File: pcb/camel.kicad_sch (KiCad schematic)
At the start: 54 parts, among them J1 Conn_01x04, J2 Conn_01x04, J3 TC2030-NL, J4 USART, J5 Conn_01x04, J6 I2C STEMMA, U1 MCP1700T-3302E/TT, U2 HX712, U3 STM32L010F4P6, U4 HX712

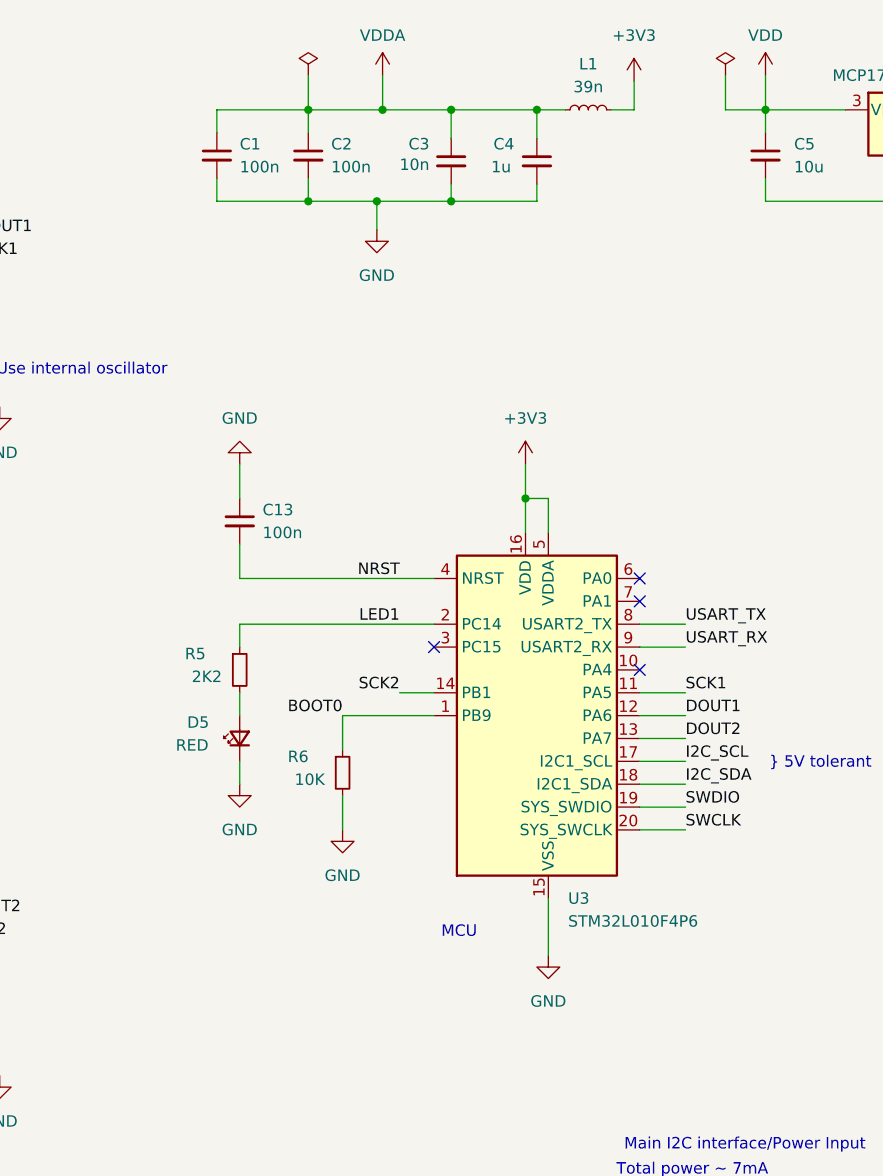
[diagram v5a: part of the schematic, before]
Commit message: updated STM32CubeMX version, updating to STM32L031F6
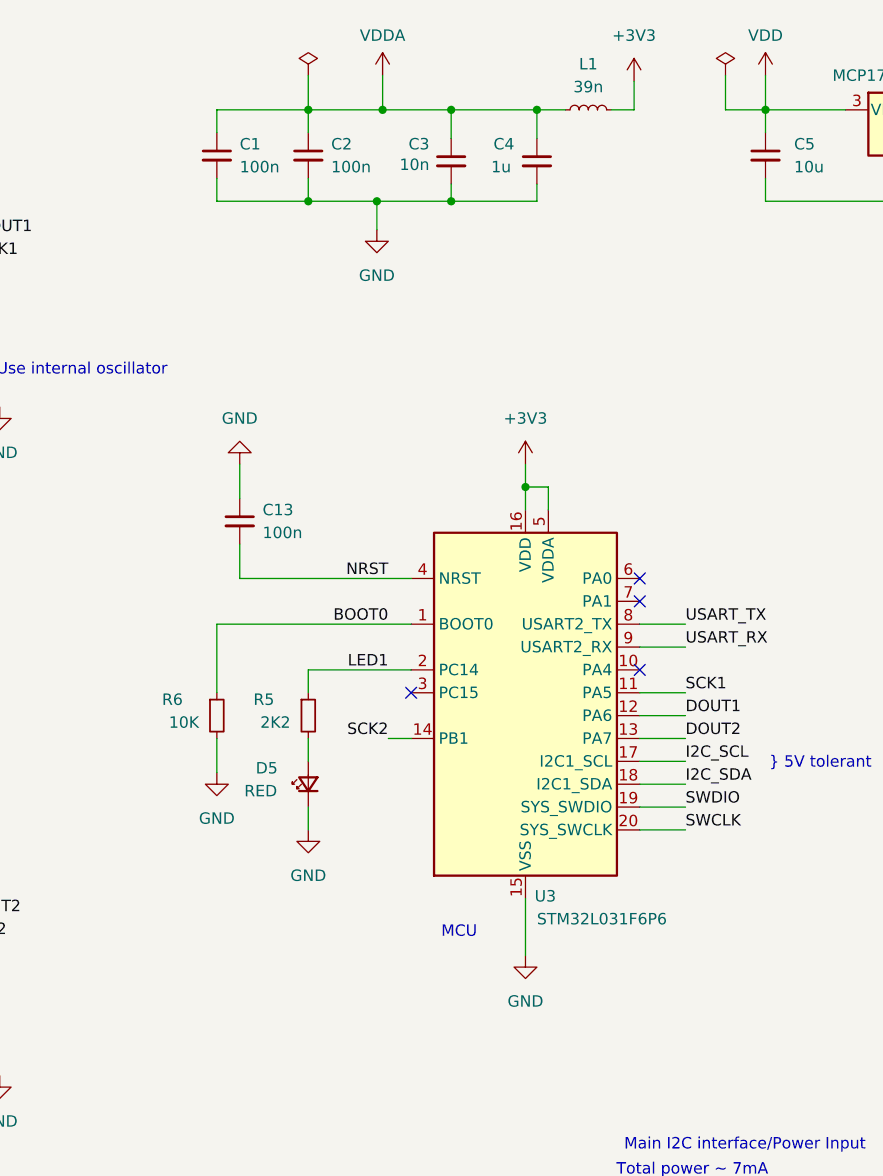
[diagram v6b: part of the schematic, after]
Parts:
- U3: value STM32L010F4P6 -> STM32L031F6P6; symbol MCU_ST_STM32L0:STM32L010F4Px -> MCU_ST_STM32L0:STM32L031F6Px; Comment 16KB 1.8V~3.6V 2KB 32MHz FLASH 16 TSSOP-20 Microcontrollers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 -> 32KB 1.8V~3.6V 8KB 32MHz FLASH 15 TSSOP-20 Microcontrollers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; LCSC C529415 -> C115208; MFRN STM32L010F4P6 -> STM32L031F6P6
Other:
- moved on the sheet: D5, R5, R6, U3

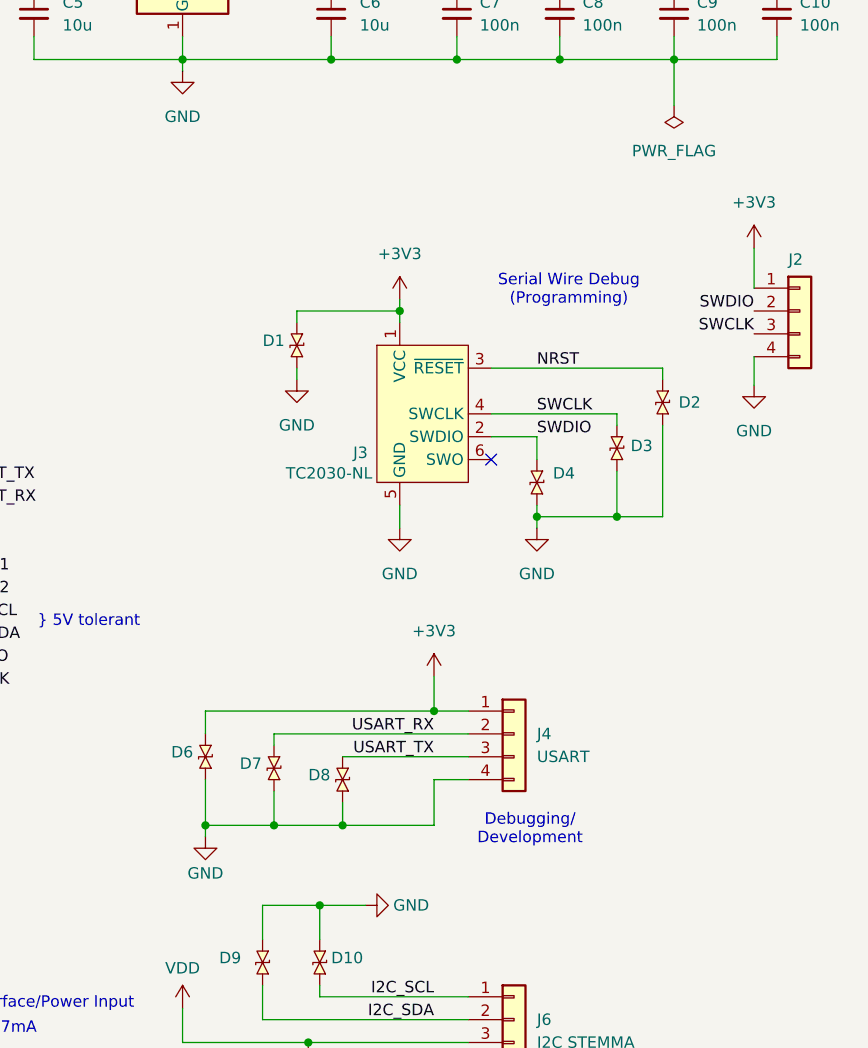
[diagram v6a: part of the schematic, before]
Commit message: version 3.0 update MCU and VDD on USART connector, prepare for JLCPCB
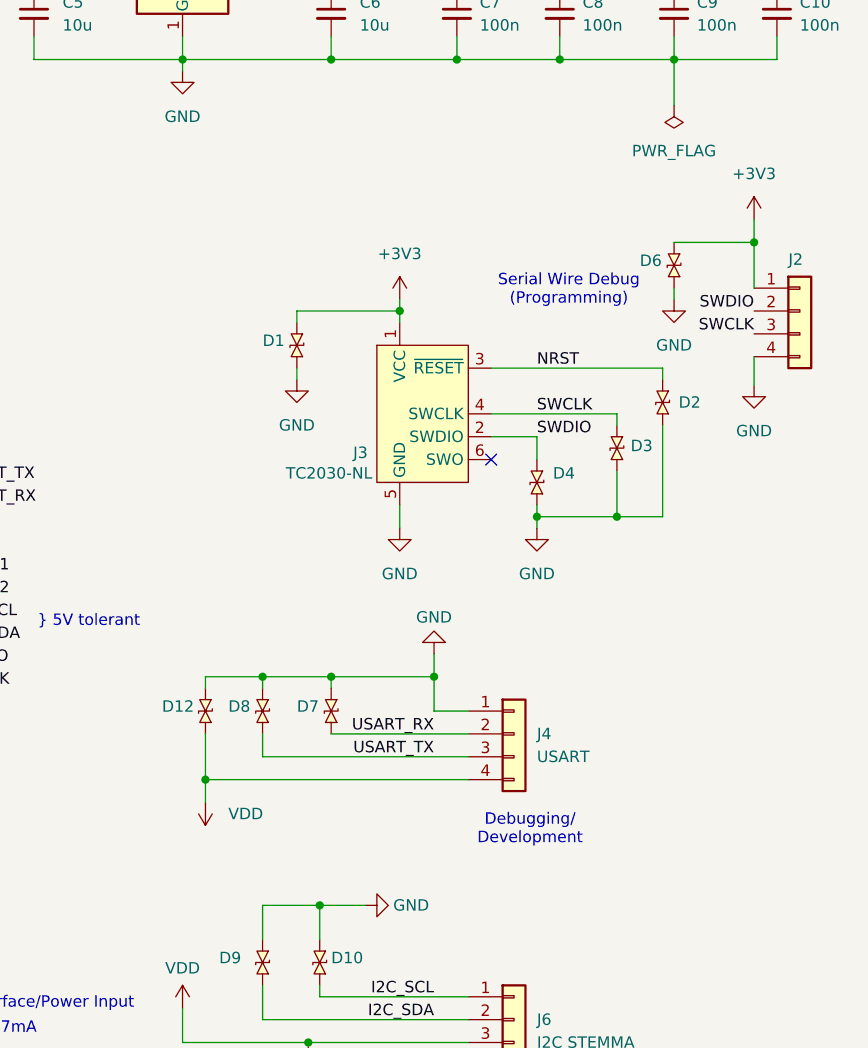
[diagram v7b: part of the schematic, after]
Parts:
- added D12: RCLAMP0521P-N, camel:X1-DFN1006-2_L1.0-W0.6-BI, symbol camel:RCLAMP0521P-N
- C4: Comment 1uF ±10% 0402 Multilayer Ceramic Capacitors MLCC - SMD/SMT 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 -> 16V 1uF X5R ±10% 0402 Multilayer Ceramic Capacitors MLCC - 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; LCSC C913556 -> C29266; MANUFACTURER Murata Electronics -> Samsung Electro-Mechanics; MFRN GRM155B31E105KA12D -> CL05A105KO5NNNC
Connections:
- net +3V3: no longer J4.1 (Pin_1)
- net GND: now also D7.1, D8.1, J4.1 (Pin_1), D12.1; no longer D7.2, D8.2, J4.4 (Pin_4)
- net USART_RX: now also D7.2; no longer D7.1
- net USART_TX: now also D8.2; no longer D8.1
- net VDD: now also J4.4 (Pin_4), D12.2
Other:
- moved on the sheet: D6, D7, D8

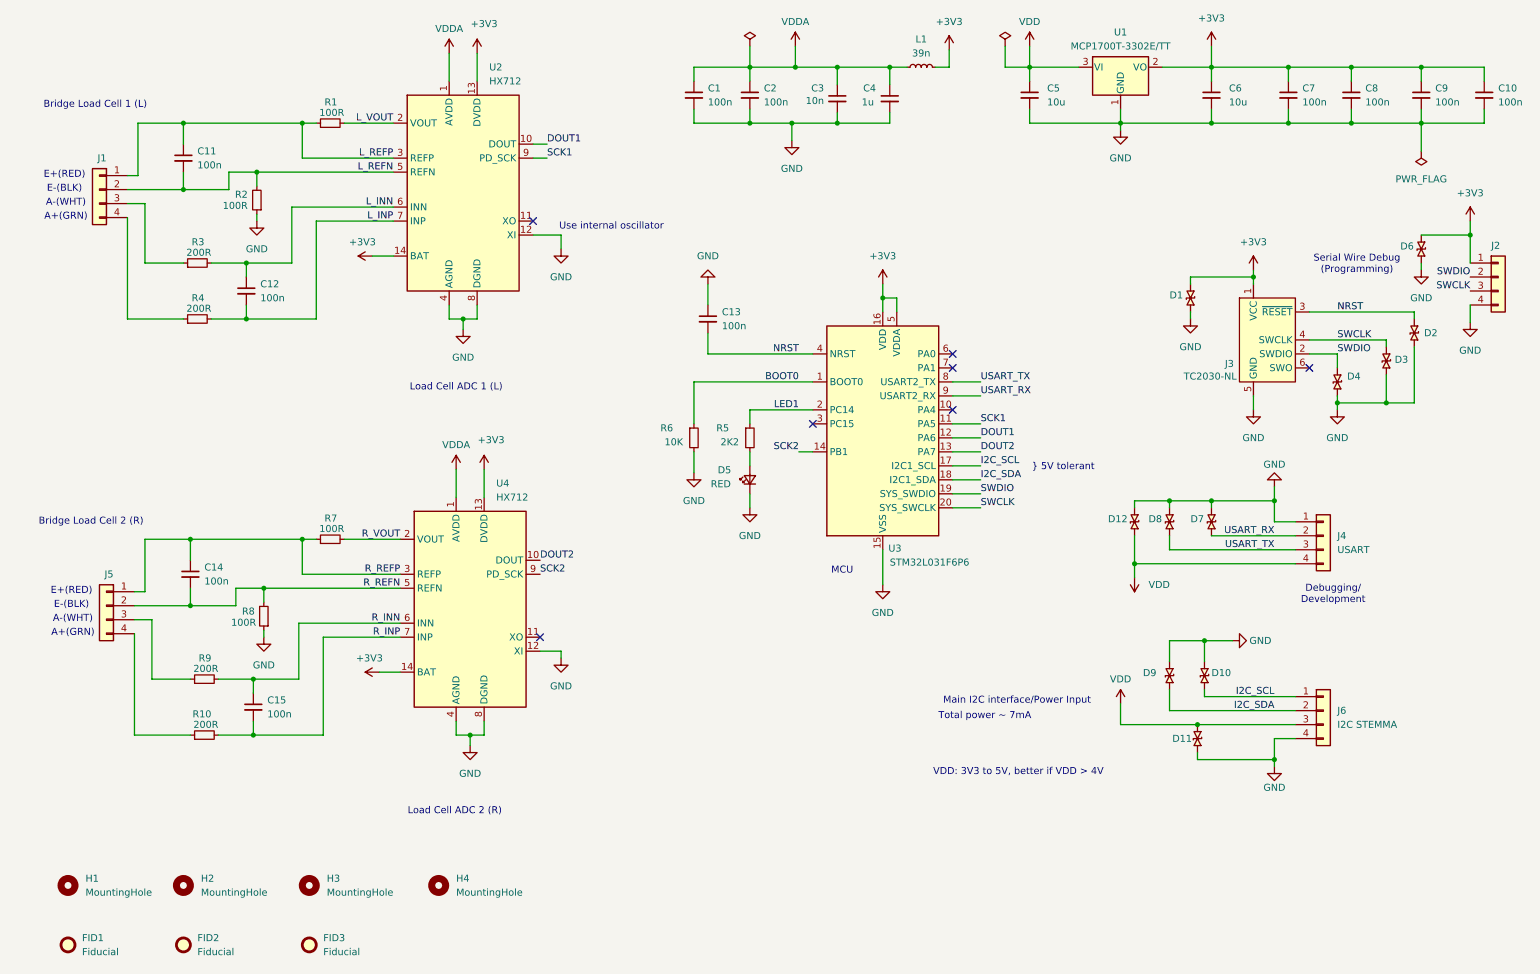
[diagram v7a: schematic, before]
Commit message: Update to STM32L071 and FreeRTOS, first stage
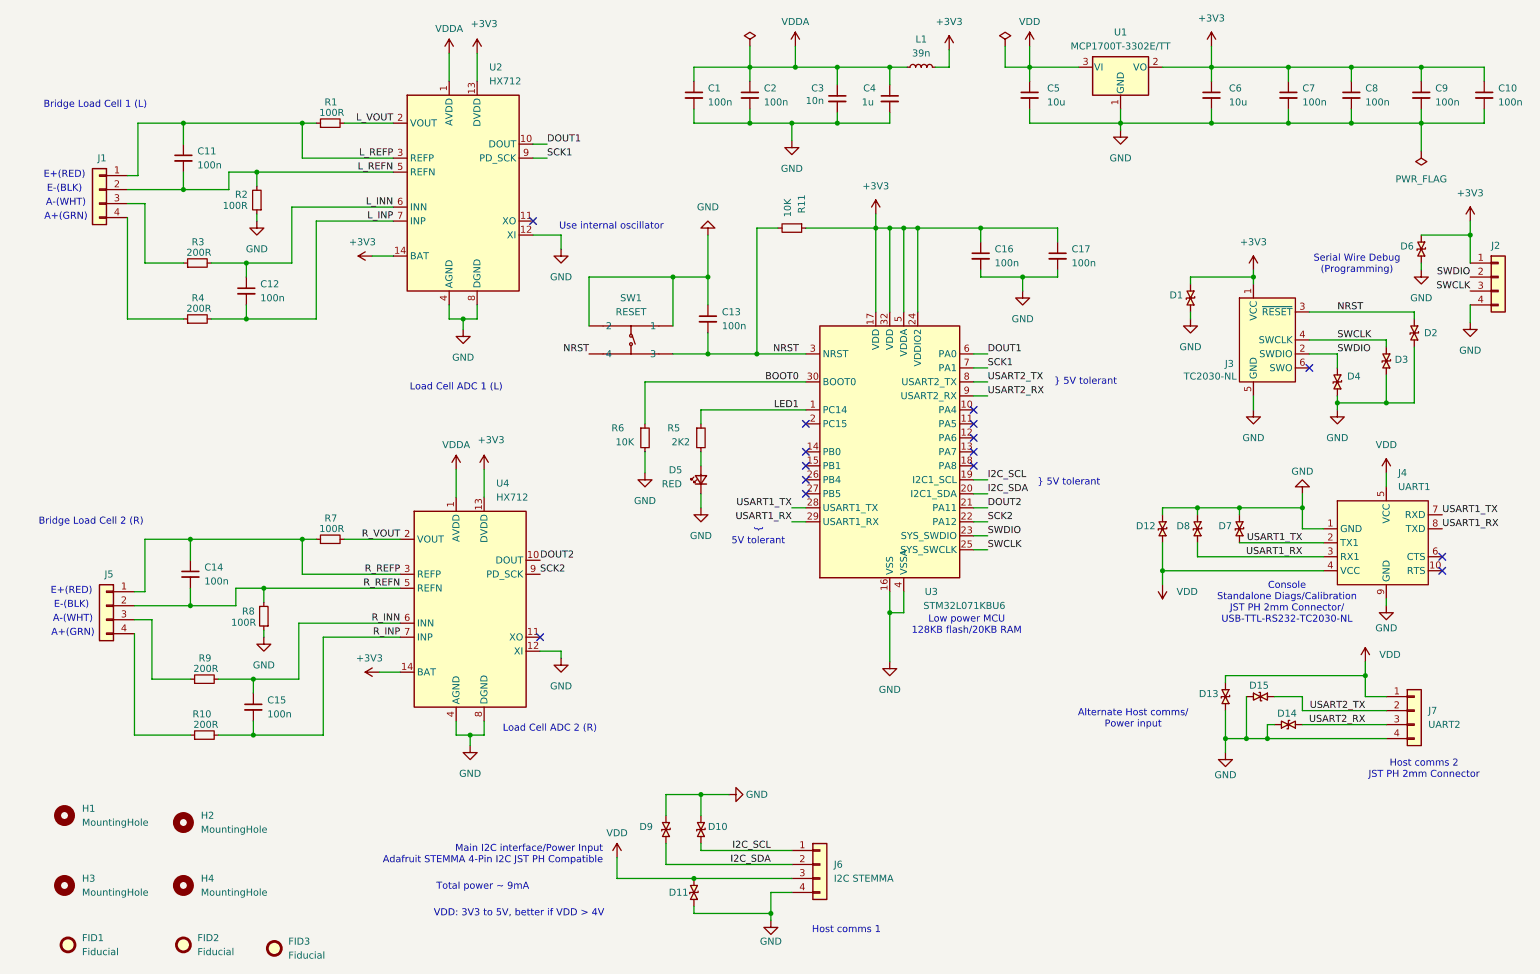
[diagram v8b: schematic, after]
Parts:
- removed U3: STM32L031F6P6, Package_SO:TSSOP-20_4.4x6.5mm_P0.65mm, symbol MCU_ST_STM32L0:STM32L031F6Px
- added C16, C17: 100n, Capacitor_SMD:C_0402_1005Metric, symbol Device:C_Small
- added D13, D14, D15: RCLAMP0521P-N, camel:X1-DFN1006-2_L1.0-W0.6-BI, symbol camel:RCLAMP0521P-N
- added J7: UART2, Connector_JST:JST_PH_S4B-PH-K_1x04_P2.00mm_Horizontal, symbol Connector_Generic:Conn_01x04
- added R11: 10K, Resistor_SMD:R_0402_1005Metric, symbol Device:R_Small
- added SW1: RESET, camel:SW-SMD_4P-L3.0-W2.6-P1.80-LS3.5, symbol camel:1TS016B-2400-0450-CT
- added U3: STM32L071KBU6, Package_DFN_QFN:QFN-32-1EP_5x5mm_P0.5mm_EP3.45x3.45mm, symbol MCU_ST_STM32L0:STM32L071KBUx
- C4: LCSC C29266 -> C29266
- J4: value USART -> UART1; footprint Connector_JST:JST_PH_S4B-PH-K_1x04_P2.00mm_Horizontal -> camel:JST_PH_S4B-PH-K_1x04_P2.00mm_Horizontal_TC-2030-IDC-NL_2x03_P1.27mm_Vertical; symbol Connector_Generic:Conn_01x04 -> camel:Conn_JST-PH_ARM_SWD_TagConnect_TC2030-NL
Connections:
- net +3V3: now also C16.1, C17.1, R11.1, U3.17 (VDD), U3.24 (VDDIO2), U3.32 (VDD), U3.5 (VDDA)
- net BOOT0: now also U3.30 (BOOT0)
- net DOUT1: now also U3.6 (PA0)
- net DOUT2: now also U3.21 (PA11)
- net GND: now also J4.9 (GND), C16.2, C17.2, D13.2, D14.1, D15.1, J7.4 (Pin_4), SW1.1, SW1.2, U3.16 (VSS), U3.31 (VSS), U3.33 (VSS), U3.4 (VSSA)
- net I2C_SCL: now also U3.19 (PA9)
- net I2C_SDA: now also U3.20 (PA10)
- net LED1: now also U3.1 (PC14)
- net NRST: now also R11.2, SW1.3, SW1.4, U3.3 (NRST)
- net SCK1: now also U3.7 (PA1)
- net SCK2: now also U3.22 (PA12)
- net SWCLK: now also U3.25 (PA14)
- net SWDIO: now also U3.23 (PA13)
- net VDD: now also J4.5 (VCC), D13.1, J7.1 (Pin_1)
- net USART_RX renamed USART1_TX
- net USART1_TX: now also J4.7 (RXD), U3.28 (PB6)
- net USART_TX renamed USART1_RX
- net USART1_RX: now also J4.8 (TXD), U3.29 (PB7)
- new net USART2_RX: D14.2, J7.3 (Pin_3), U3.9 (PA3)
- new net USART2_TX: D15.2, J7.2 (Pin_2), U3.8 (PA2)
- no-connect marks 7 -> 15
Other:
- note added: "5V tolerant"
- note added: "Alternate Host comms/ Power input"
- note added: "Console Standalone Diags/Calibration JST PH 2mm Connector/ USB-TTL-RS232-TC2030-NL"
- note added: "Host comms 1"
- note added: "Host comms 2 JST PH 2mm Connector"
- note added: "Low power MCU 128KB flash/20KB RAM"
- note added: "Main I2C interface/Power Input Adafruit STEMMA 4-Pin I2C JST PH Compatible"
- note added: "Total power ~ 9mA"
- note added: "{"
- note removed: "Debugging/ Development"
- note removed: "MCU"
- note removed: "Main I2C interface/Power Input"
- note removed: "Total power ~ 7mA"
- moved on the sheet: D10, D11, D12, D5, D7, D8, D9, FID3, H1, H2, H3, H4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
